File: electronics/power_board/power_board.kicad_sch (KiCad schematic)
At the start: 43 parts, among them J1 Vin, J2 I2C_low, J3 I2C_high, J4 3.3V out, J5 5V out, Q1 2N7002E, Q2 2N7002E, U1 TPS54228, U2 TPS54228

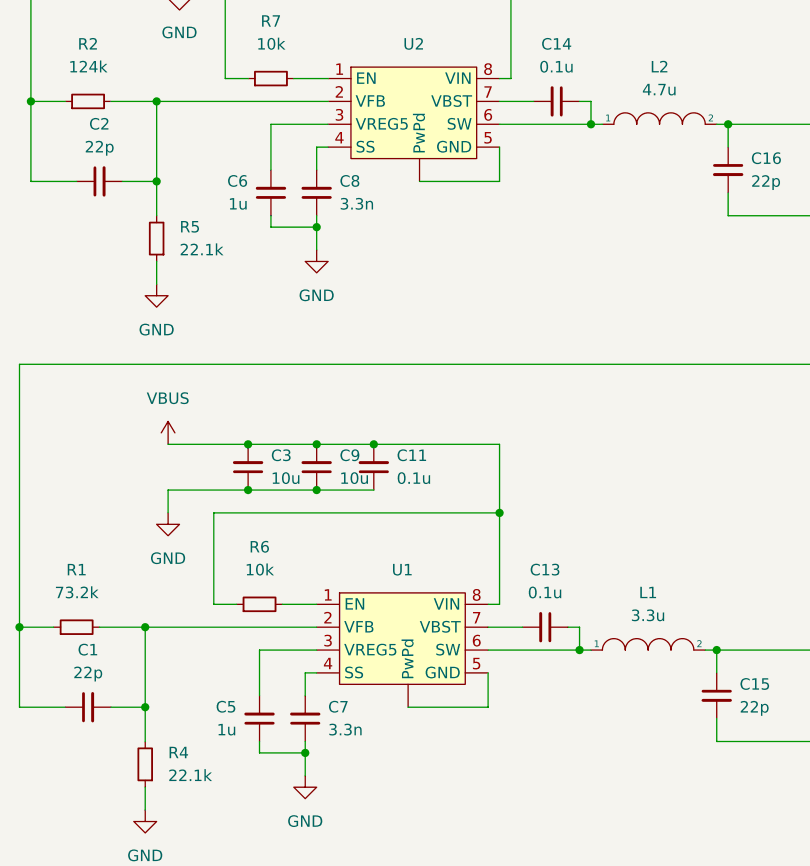
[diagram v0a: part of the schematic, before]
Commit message: power board pcb not finished
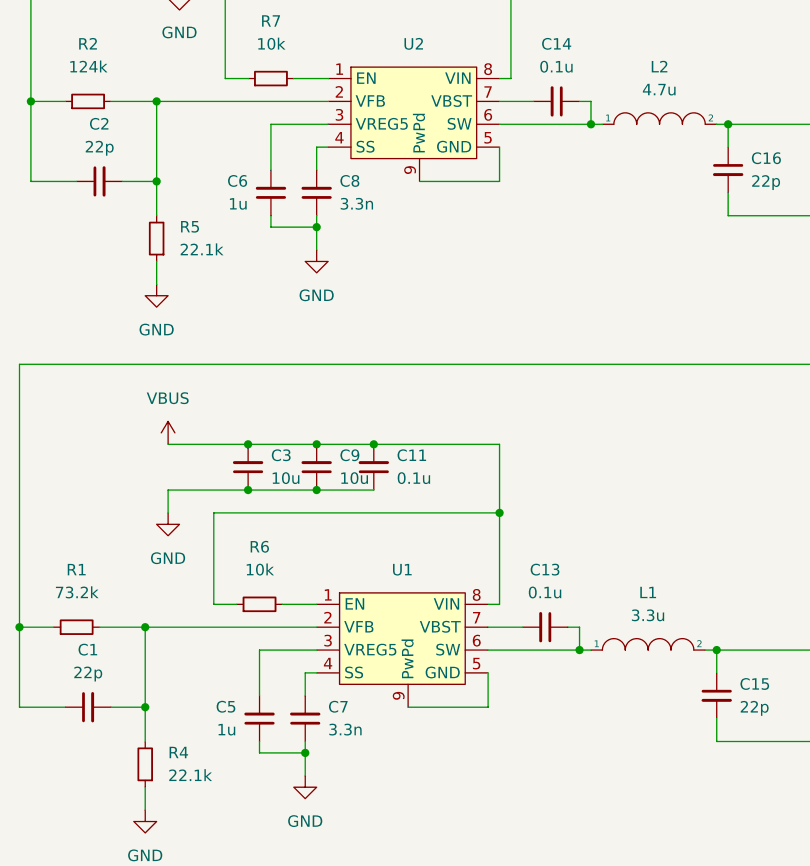
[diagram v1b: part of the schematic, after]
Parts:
- L1, L2: footprint (none) -> Inductor_SMD:L_Neosid_SM-NE127_HandSoldering
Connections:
- net at U1.5 (GND): now also U1.9 (PwPd); no longer U1. (PwPd)
- net at U2.5 (GND): now also U2.9 (PwPd); no longer U2. (PwPd)
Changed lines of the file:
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@@
       (effects (font (size 1.27 1.27)) hide)
     )
-    (pin "")
     (pin "1")
     (pin "2")
@@
     (pin "7")
     (pin "8")
+    (pin "9")
   )
   (symbol (lib_id "Device:C_Small") (at 129.54 60.96 270) (unit 1)
@@
     (property "Reference" "L1" (id 0) (at 139.7 115.57 0))
     (property "Value" "3.3u" (id 1) (at 139.7 118.11 0))
-    (property "Footprint" "" (id 2) (at 139.7 121.92 0)
-      (effects (font (size 1.27 1.27)) hide)
-    )
-    (property "Datasheet" "~" (id 3) (at 139.7 121.92 0)
+    (property "Footprint" "Inductor_SMD:L_Neosid_SM-NE127_HandSoldering" (id 2) (at 139.7 121.92 0)
+      (effects (font (size 1.27 1.27)) hide)
+    )
+    (property "Datasheet" "https://www.tme.eu/pl/details/hpi0530-3r3/dlawiki-smd-mocy/ferrocore/" (id 3) (at 139.7 121.92 0)
       (effects (font (size 1.27 1.27)) hide)
     )
@@
     (pin "1")
   )
-  (symbol (lib_id "Samolot:TPS54228") (at 113.03 66.04 0) (unit 1)
+  (symbol (lib_name "TPS54228_1") (lib_id "Samolot:TPS54228") (at 113.03 66.04 0) (unit 1)
     (in_bom yes) (on_board yes) (fields_autoplaced)
     (property "Reference" "U2" (id 0) (at 113.665 54.61 0))
@@
       (effects (font (size 1.27 1.27)) hide)
     )
-    (pin "")
     (pin "1")
     (pin "2")
@@
     (pin "7")
     (pin "8")
+    (pin "9")
   )
   (symbol (lib_id "Device:C_Small") (at 147.32 127 0) (unit 1)
@@
     (property "Reference" "L2" (id 0) (at 140.97 57.15 0))
     (property "Value" "4.7u" (id 1) (at 140.97 59.69 0))
-    (property "Footprint" "" (id 2) (at 140.97 63.5 0)
-      (effects (font (size 1.27 1.27)) hide)
-    )
-    (property "Datasheet" "~" (id 3) (at 140.97 63.5 0)
+    (property "Footprint" "Inductor_SMD:L_Neosid_SM-NE127_HandSoldering" (id 2) (at 140.97 63.5 0)
+      (effects (font (size 1.27 1.27)) hide)
+    )
+    (property "Datasheet" "https://www.tme.eu/pl/details/hpi0530-4r7/dlawiki-smd-mocy/ferrocore/" (id 3) (at 140.97 63.5 0)
       (effects (font (size 1.27 1.27)) hide)
     )
@@
     )
     (path "/788ebf59-d091-4ef6-93f5-5fb436e5a6c3"
-      (reference "L1") (unit 1) (value "3.3u") (footprint "")
+      (reference "L1") (unit 1) (value "3.3u") (footprint "Inductor_SMD:L_Neosid_SM-NE127_HandSoldering")
     )
     (path "/f1cf2019-4095-47c2-9b47-2e2e1e9551af"
-      (reference "L2") (unit 1) (value "4.7u") (footprint "")
+      (reference "L2") (unit 1) (value "4.7u") (footprint "Inductor_SMD:L_Neosid_SM-NE127_HandSoldering")
     )
     (path "/f746787f-ad7f-4934-9aa7-1edb236028a7"

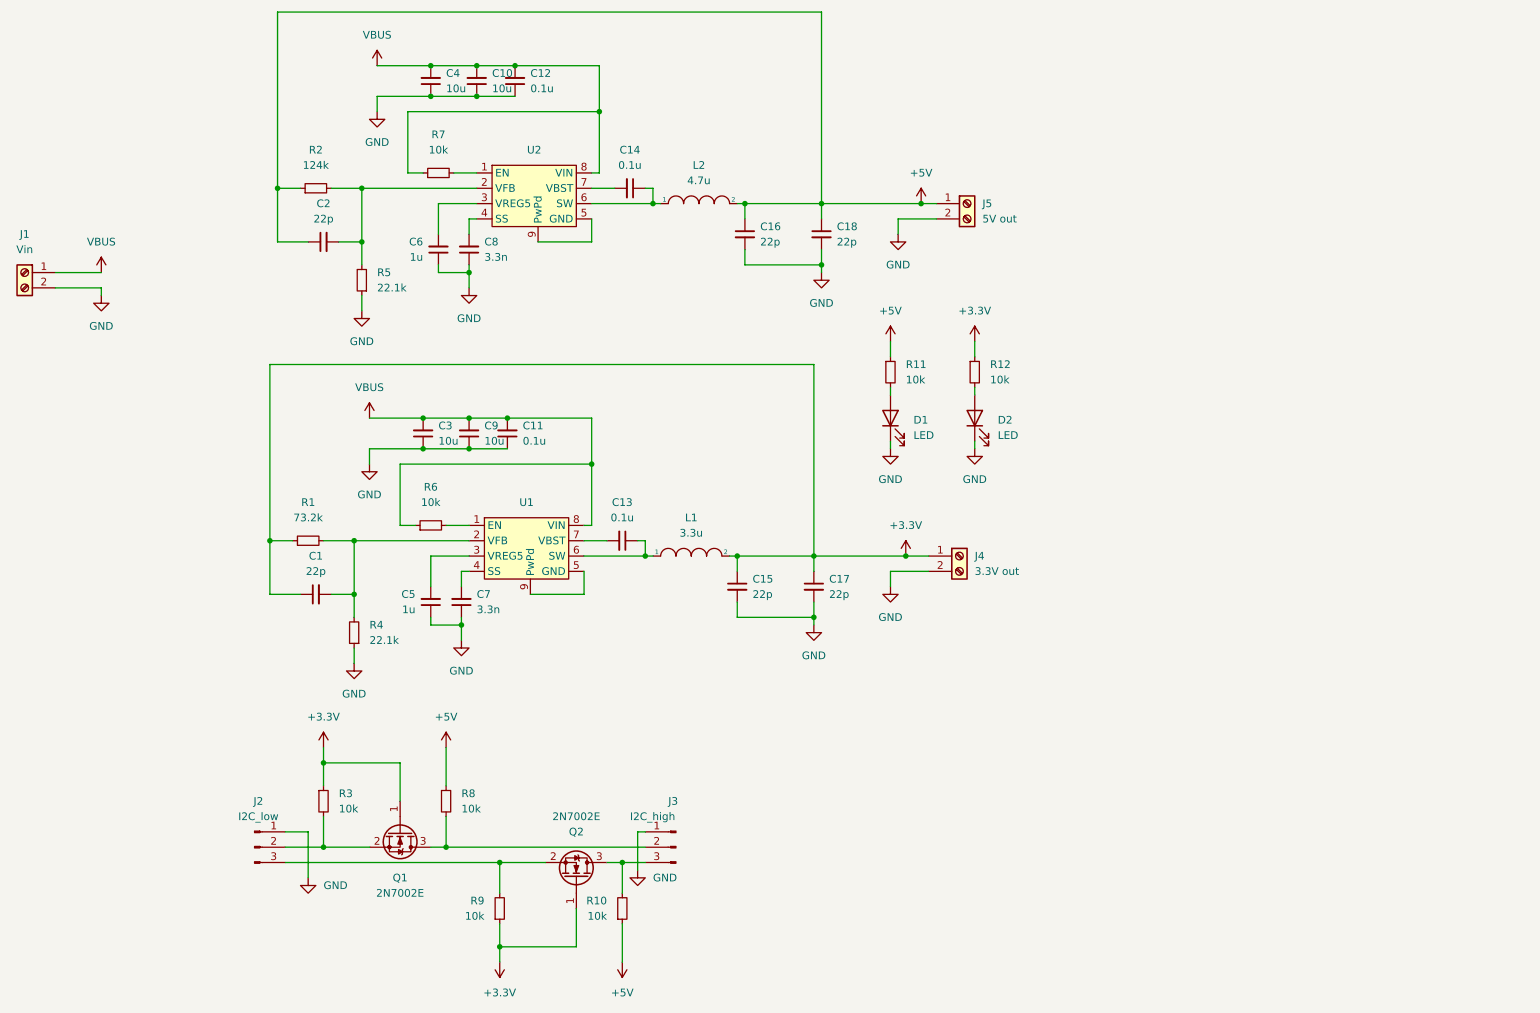
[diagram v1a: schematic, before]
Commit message: links fixed
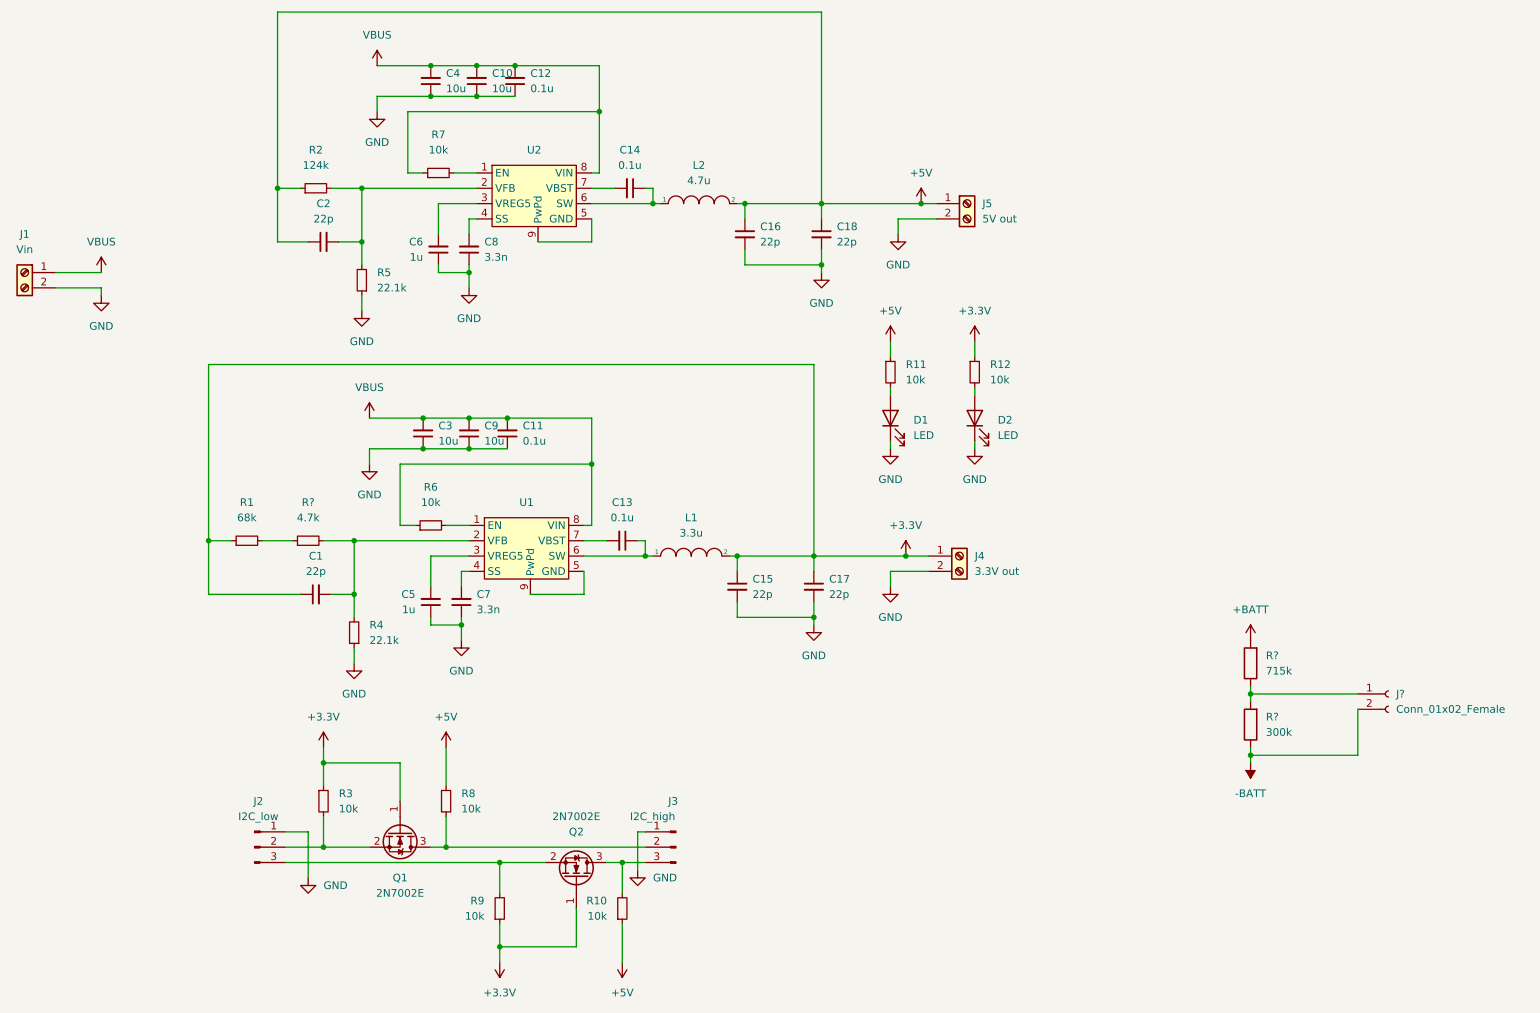
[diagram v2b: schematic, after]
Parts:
- added J?: Conn_01x02_Female, symbol Connector:Conn_01x02_Female
- added R?: 300k, Resistor_SMD:R_1206_3216Metric_Pad1.30x1.75mm_HandSolder, symbol Device:R
- added R?: 4.7k, Resistor_SMD:R_1206_3216Metric_Pad1.30x1.75mm_HandSolder, symbol Device:R_Small
- added R?: 715k, Resistor_SMD:R_1206_3216Metric_Pad1.30x1.75mm_HandSolder, symbol Device:R
- R1: value 73.2k -> 68k
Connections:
- net at C1.2, R4.2, U1.2 (VFB): now also R?.2; no longer R1.2
- new net: J?.1 (Pin_1), R?.1, R?.2
- new net: R1.2, R?.1
- new net +BATT: R?.2
- new net -BATT: J?.2 (Pin_2), R?.1
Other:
- moved on the sheet: R1

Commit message: futher fixes
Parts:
- gave numbers to parts that had none: 4
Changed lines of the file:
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@@
   (symbol (lib_id "Connector:Conn_01x02_Female") (at 255.27 144.78 0) (unit 1)
     (in_bom yes) (on_board yes) (fields_autoplaced)
-    (property "Reference" "J?" (id 0) (at 256.54 144.7799 0)
+    (property "Reference" "J6" (id 0) (at 256.54 144.7799 0)
       (effects (font (size 1.27 1.27)) (justify left))
     )
@@
   (symbol (lib_id "Device:R") (at 232.41 149.86 180) (unit 1)
     (in_bom yes) (on_board yes) (fields_autoplaced)
-    (property "Reference" "R?" (id 0) (at 234.95 148.5899 0)
+    (property "Reference" "R15" (id 0) (at 234.95 148.5899 0)
       (effects (font (size 1.27 1.27)) (justify right))
     )
@@
   (symbol (lib_id "Device:R_Small") (at 76.2 119.38 90) (unit 1)
     (in_bom yes) (on_board yes) (fields_autoplaced)
-    (property "Reference" "R?" (id 0) (at 76.2 113.03 90))
+    (property "Reference" "R13" (id 0) (at 76.2 113.03 90))
     (property "Value" "4.7k" (id 1) (at 76.2 115.57 90))
     (property "Footprint" "Resistor_SMD:R_1206_3216Metric_Pad1.30x1.75mm_HandSolder" (id 2) (at 76.2 119.38 0)
@@
   (symbol (lib_id "power:+BATT") (at 232.41 135.89 0) (unit 1)
     (in_bom yes) (on_board yes) (fields_autoplaced)
-    (property "Reference" "#PWR?" (id 0) (at 232.41 139.7 0)
+    (property "Reference" "#PWR027" (id 0) (at 232.41 139.7 0)
       (effects (font (size 1.27 1.27)) hide)
     )
@@
   (symbol (lib_id "Device:R") (at 232.41 139.7 180) (unit 1)
     (in_bom yes) (on_board yes) (fields_autoplaced)
-    (property "Reference" "R?" (id 0) (at 234.95 138.4299 0)
+    (property "Reference" "R14" (id 0) (at 234.95 138.4299 0)
       (effects (font (size 1.27 1.27)) (justify right))
     )
@@
   (symbol (lib_id "power:-BATT") (at 232.41 156.21 180) (unit 1)
     (in_bom yes) (on_board yes) (fields_autoplaced)
-    (property "Reference" "#PWR?" (id 0) (at 232.41 152.4 0)
+    (property "Reference" "#PWR028" (id 0) (at 232.41 152.4 0)
       (effects (font (size 1.27 1.27)) hide)
     )
@@
     )
     (path "/cca7b222-2dee-447f-a76f-f92f0b38e7c4"
-      (reference "#PWR?") (unit 1) (value "+BATT") (footprint "")
+      (reference "#PWR027") (unit 1) (value "+BATT") (footprint "")
     )
     (path "/e332f373-6800-48f8-a1ff-30fe70e47d14"
-      (reference "#PWR?") (unit 1) (value "-BATT") (footprint "")
+      (reference "#PWR028") (unit 1) (value "-BATT") (footprint "")
     )
     (path "/f2bf90a1-3320-4265-a7bd-e344504722fa"
@@
     )
     (path "/4e844c55-fbf1-4a1e-9a50-fe8f7e8bf095"
-      (reference "J?") (unit 1) (value "Conn_01x02_Female") (footprint "")
+      (reference "J6") (unit 1) (value "Conn_01x02_Female") (footprint "")
     )
     (path "/788ebf59-d091-4ef6-93f5-5fb436e5a6c3"
@@
       (reference "R12") (unit 1) (value "10k") (footprint "Resistor_SMD:R_1206_3216Metric_Pad1.30x1.75mm_HandSolder")
     )
+    (path "/b1232db4-f029-47fc-ad5d-7e861867252f"
+      (reference "R13") (unit 1) (value "4.7k") (footprint "Resistor_SMD:R_1206_3216Metric_Pad1.30x1.75mm_HandSolder")
+    )
+    (path "/d86d6d81-22aa-419c-b613-48d8956dd268"
+      (reference "R14") (unit 1) (value "715k") (footprint "Resistor_SMD:R_1206_3216Metric_Pad1.30x1.75mm_HandSolder")
+    )
     (path "/ae2de93b-9af6-4bde-a00f-2d279a709159"
-      (reference "R?") (unit 1) (value "300k") (footprint "Resistor_SMD:R_1206_3216Metric_Pad1.30x1.75mm_HandSolder")
-    )
-    (path "/b1232db4-f029-47fc-ad5d-7e861867252f"
-      (reference "R?") (unit 1) (value "4.7k") (footprint "Resistor_SMD:R_1206_3216Metric_Pad1.30x1.75mm_HandSolder")
-    )
-    (path "/d86d6d81-22aa-419c-b613-48d8956dd268"
-      (reference "R?") (unit 1) (value "715k") (footprint "Resistor_SMD:R_1206_3216Metric_Pad1.30x1.75mm_HandSolder")
+      (reference "R15") (unit 1) (value "300k") (footprint "Resistor_SMD:R_1206_3216Metric_Pad1.30x1.75mm_HandSolder")
     )
     (path "/28d3855e-a698-4a58-ab22-353570200327"

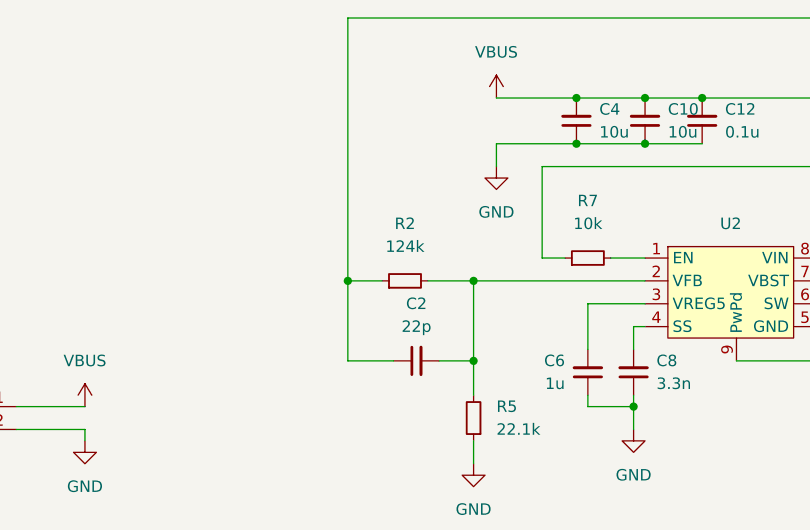
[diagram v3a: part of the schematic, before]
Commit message: powerboard link fix
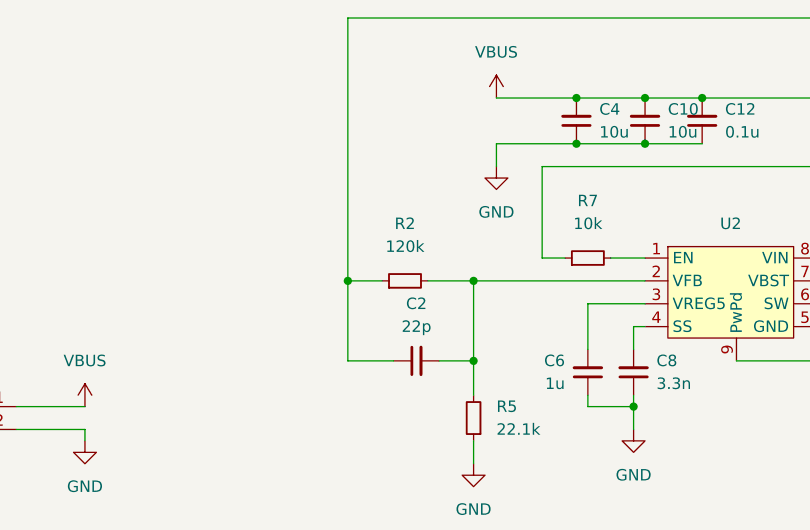
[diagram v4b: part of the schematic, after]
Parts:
- R2: value 124k -> 120k
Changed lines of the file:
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@@
     (in_bom yes) (on_board yes) (fields_autoplaced)
     (property "Reference" "R2" (id 0) (at 77.47 54.61 90))
-    (property "Value" "124k" (id 1) (at 77.47 57.15 90))
+    (property "Value" "120k" (id 1) (at 77.47 57.15 90))
     (property "Footprint" "Resistor_SMD:R_1206_3216Metric_Pad1.30x1.75mm_HandSolder" (id 2) (at 77.47 60.96 0)
       (effects (font (size 1.27 1.27)) hide)
     )
-    (property "Datasheet" "https://www.tme.eu/pl/details/rc1206fr-07124kl/rezystory-smd-1206/yageo/" (id 3) (at 77.47 60.96 0)
+    (property "Datasheet" "https://www.tme.eu/pl/details/smd1206-120k/rezystory-smd-1206/royal-ohm/1206s4j0124t5e/" (id 3) (at 77.47 60.96 0)
       (effects (font (size 1.27 1.27)) hide)
     )
@@
       (effects (font (size 1.27 1.27)) hide)
     )
-    (property "Datasheet" "https://www.tme.eu/pl/details/2n7002e-7-f/tranzystory-z-kanalem-n-smd/diodes-incorporated/" (id 3) (at 66.04 119.38 0)
+    (property "Datasheet" "https://www.tme.eu/pl/details/smd1206-68k-1%25/rezystory-smd-1206/royal-ohm/1206s4f6802t5e/" (id 3) (at 66.04 119.38 0)
       (effects (font (size 1.27 1.27)) hide)
     )
@@
       (effects (font (size 1.27 1.27)) hide)
     )
-    (property "Datasheet" "https://www.tme.eu/pl/details/2n7002e-7-f/tranzystory-z-kanalem-n-smd/diodes-incorporated/" (id 3) (at 76.2 119.38 0)
+    (property "Datasheet" "https://www.tme.eu/pl/details/rc1206fr-074k7/rezystory-smd-1206/yageo/rc1206fr-074k7l/" (id 3) (at 76.2 119.38 0)
       (effects (font (size 1.27 1.27)) hide)
     )
@@
       (effects (font (size 1.27 1.27) italic) (justify left) hide)
     )
-    (property "Datasheet" "http://www.diodes.com/assets/Datasheets/ds30376.pdf" (id 3) (at 120.65 175.26 0)
+    (property "Datasheet" "https://www.tme.eu/pl/details/2n7002e-7-f/tranzystory-z-kanalem-n-smd/diodes-incorporated/" (id 3) (at 120.65 175.26 0)
       (effects (font (size 1.27 1.27)) (justify left) hide)
     )
@@
       (effects (font (size 1.27 1.27) italic) (justify left) hide)
     )
-    (property "Datasheet" "http://www.diodes.com/assets/Datasheets/ds30376.pdf" (id 3) (at 91.44 167.64 0)
+    (property "Datasheet" "https://www.tme.eu/pl/details/2n7002e-7-f/tranzystory-z-kanalem-n-smd/diodes-incorporated/" (id 3) (at 91.44 167.64 0)
       (effects (font (size 1.27 1.27)) (justify left) hide)
     )
@@
     )
     (path "/23d7a342-655b-4b8d-bf9a-a43d611a82f3"
-      (reference "R2") (unit 1) (value "124k") (footprint "Resistor_SMD:R_1206_3216Metric_Pad1.30x1.75mm_HandSolder")
+      (reference "R2") (unit 1) (value "120k") (footprint "Resistor_SMD:R_1206_3216Metric_Pad1.30x1.75mm_HandSolder")
     )
     (path "/35bcb39c-7d81-4035-be20-85bd3a5d295d"

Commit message: power board finished
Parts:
- removed J2: I2C_low, Connector_PinSocket_2.54mm:PinSocket_1x03_P2.54mm_Vertical, symbol Connector:Conn_01x03_Male
- removed J3: I2C_high, Connector_PinSocket_2.54mm:PinSocket_1x03_P2.54mm_Vertical, symbol Connector:Conn_01x03_Male
- removed J6: Conn_01x02_Female, symbol Connector:Conn_01x02_Female
- removed Q1, Q2: 2N7002E, Package_TO_SOT_SMD:SOT-23, symbol Transistor_FET:2N7002E
- removed R10, R3, R8, R9: 10k, Resistor_SMD:R_1206_3216Metric_Pad1.30x1.75mm_HandSolder, symbol Device:R_Small
- removed R14: 715k, Resistor_SMD:R_1206_3216Metric_Pad1.30x1.75mm_HandSolder, symbol Device:R
- removed R15: 300k, Resistor_SMD:R_1206_3216Metric_Pad1.30x1.75mm_HandSolder, symbol Device:R
- added J7: Vin, moje:ARK, symbol Connector:Screw_Terminal_01x02
- added R16: 4.7k, Resistor_SMD:R_1206_3216Metric_Pad1.30x1.75mm_HandSolder, symbol Device:R_Small
- C15, C16, C17, C18: value 22p -> 22u; footprint Capacitor_SMD:C_1206_3216Metric_Pad1.33x1.80mm_HandSolder -> Capacitor_SMD:CP_Elec_6.3x5.4; symbol Device:C_Small -> Device:C_Polarized_Small
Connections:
- net GND: now also U1.5 (GND), U1.9 (PwPd), U2.5 (GND), U2.9 (PwPd), J7.2 (Pin_2)
- net at C2.2, R5.2, U2.2 (VFB): now also R16.2; no longer R2.2
- net VBUS renamed VCC
- net VCC: no longer C10.2, C12.2, C4.2, R7.1, U2.8 (VIN)
- new net: R16.1, R2.2
- new net VAA: C10.2, C12.2, C4.2, J7.1 (Pin_1), R7.1, U2.8 (VIN)
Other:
- moved on the sheet: R2
